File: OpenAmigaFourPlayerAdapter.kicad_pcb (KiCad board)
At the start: 2 copper layers, 51.8 x 26.4 mm, 6 parts, among them J1 F25HP, J3 F09HP, J4 F09HP, J99 OSHW_LOGO

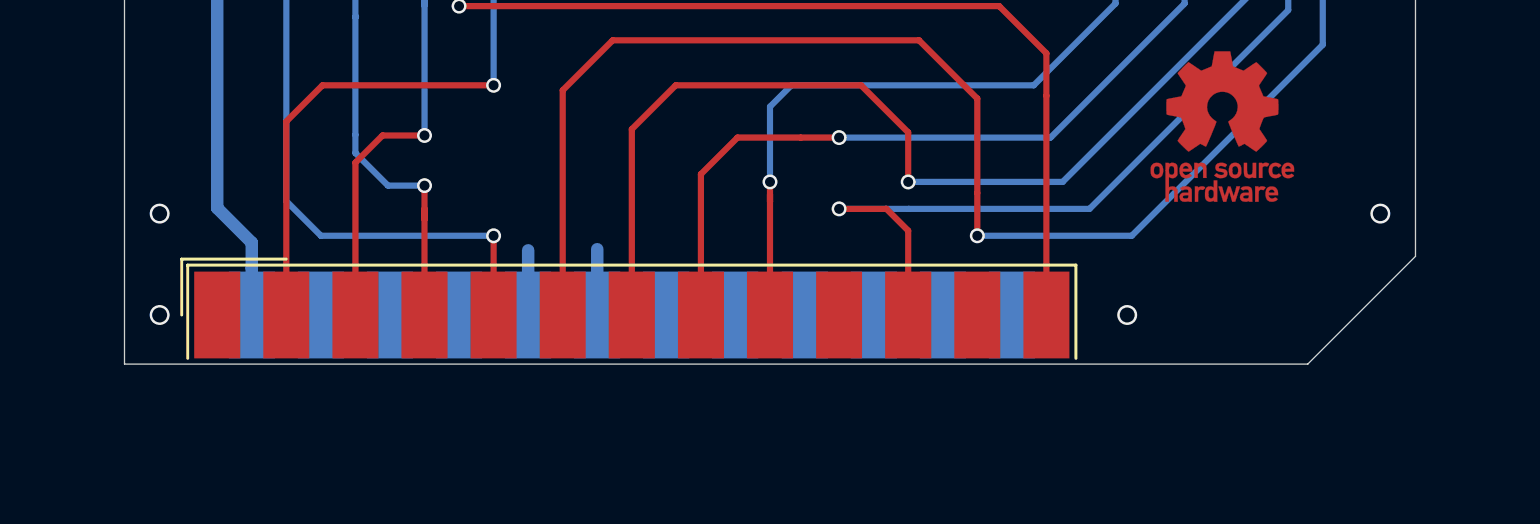
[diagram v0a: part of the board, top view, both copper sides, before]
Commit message: Improve ground stitching
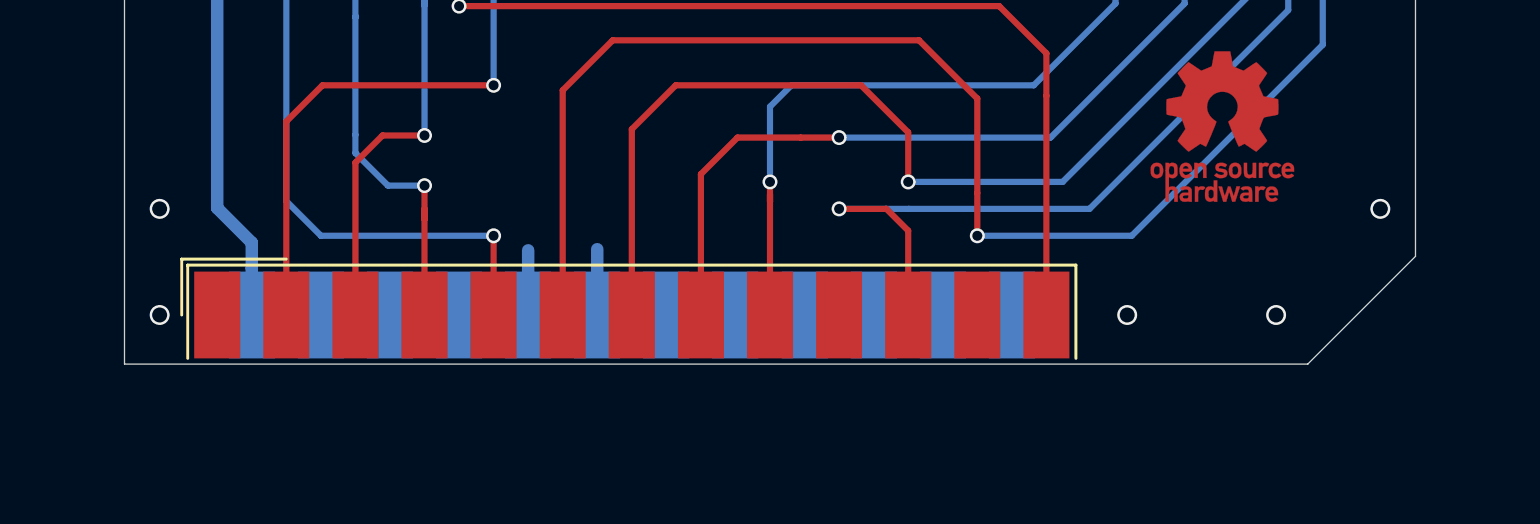
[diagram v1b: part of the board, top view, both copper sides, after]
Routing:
- net /gnd: vias 9 -> 10
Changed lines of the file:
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@@
     (thickness 1.6)
     (drawings 11)
-    (tracks 139)
+    (tracks 140)
     (zones 0)
     (modules 6)
@@
   (title_block
     (title OpenAmigaFourPlayerAdapter)
-    (date 2020-02-18)
+    (date 2020-02-22)
     (rev 2git)
     (company SukkoPera)
@@
     (effects (font (size 1 1) (thickness 0.15)) (justify mirror))
   )
-  (gr_text V2 (at 175.514 112.268) (layer B.SilkS)
+  (gr_text V2 (at 166.878 112.395) (layer B.SilkS)
     (effects (font (size 1 1) (thickness 0.15)) (justify mirror))
   )
@@
   (segment (start 145.1505 111.6965) (end 145.1505 109.1035) (width 0.5) (layer Bottom) (net 13) (status 10))
   (via (at 179.312415 89.2175) (size 0.8) (drill 0.6) (layers Top Bottom) (net 13))
-  (via (at 130.377833 107.6325) (size 0.8) (drill 0.6) (layers Top Bottom) (net 13))
-  (via (at 179.312415 107.6325) (size 0.8) (drill 0.6) (layers Top Bottom) (net 13))
+  (via (at 130.377833 107.442) (size 0.8) (drill 0.6) (layers Top Bottom) (net 13))
+  (via (at 179.312415 107.442) (size 0.8) (drill 0.6) (layers Top Bottom) (net 13))
   (via (at 130.377833 111.6965) (size 0.8) (drill 0.6) (layers Top Bottom) (net 13))
   (via (at 169.164 111.6965) (size 0.8) (drill 0.6) (layers Top Bottom) (net 13))
@@
   (segment (start 170.0805 89.2175) (end 170.0805 92.1625) (width 0.5) (layer Bottom) (net 13) (status 10))
   (via (at 163.1555 89.2175) (size 0.8) (drill 0.6) (layers Top Bottom) (net 13))
+  (via (at 175.133 111.6965) (size 0.8) (drill 0.6) (layers Top Bottom) (net 13))
   (via (at 168.6955 94.742) (size 0.6) (drill 0.4) (layers Top Bottom) (net 14))
   (segment (start 168.6955 89.2175) (end 168.6955 92.7015) (width 0.25) (layer Top) (net 14) (status 10))

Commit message: Ready for V2
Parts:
- moved J99 1.70 mm to (172.8, 102.4)
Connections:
- J1 pad 17: (no net) -> /gnd
- J1 pad 20: (no net) -> /gnd
- J1 pad 21: (no net) -> /gnd
- J1 pad 22: (no net) -> /gnd
- J1 pad 23: (no net) -> /gnd
- J1 pad 24: (no net) -> /gnd
- J1 pad 25: (no net) -> /gnd
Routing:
- net /gnd: track 11.1 -> 31.6 mm, vias 10 -> 11
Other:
- outline, holes or cut-outs redrawn
